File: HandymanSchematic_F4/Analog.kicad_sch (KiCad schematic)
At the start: 38 parts, among them Q1 BC847, U2 TL074, U6 TL072

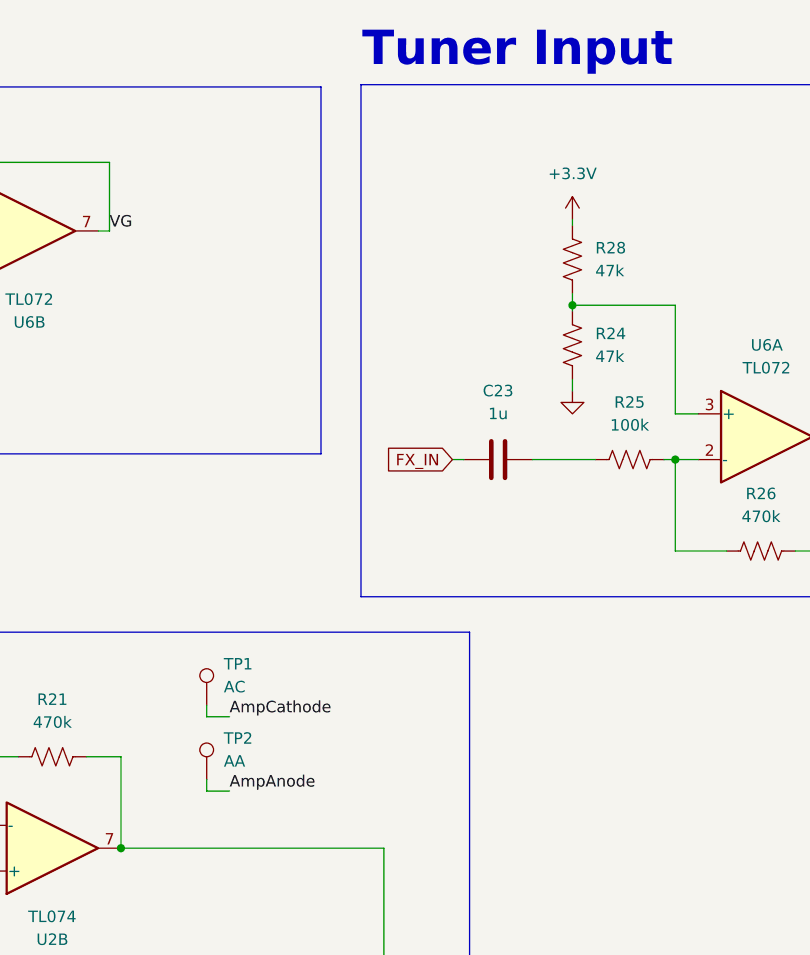
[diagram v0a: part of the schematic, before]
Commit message: schem changes for new display
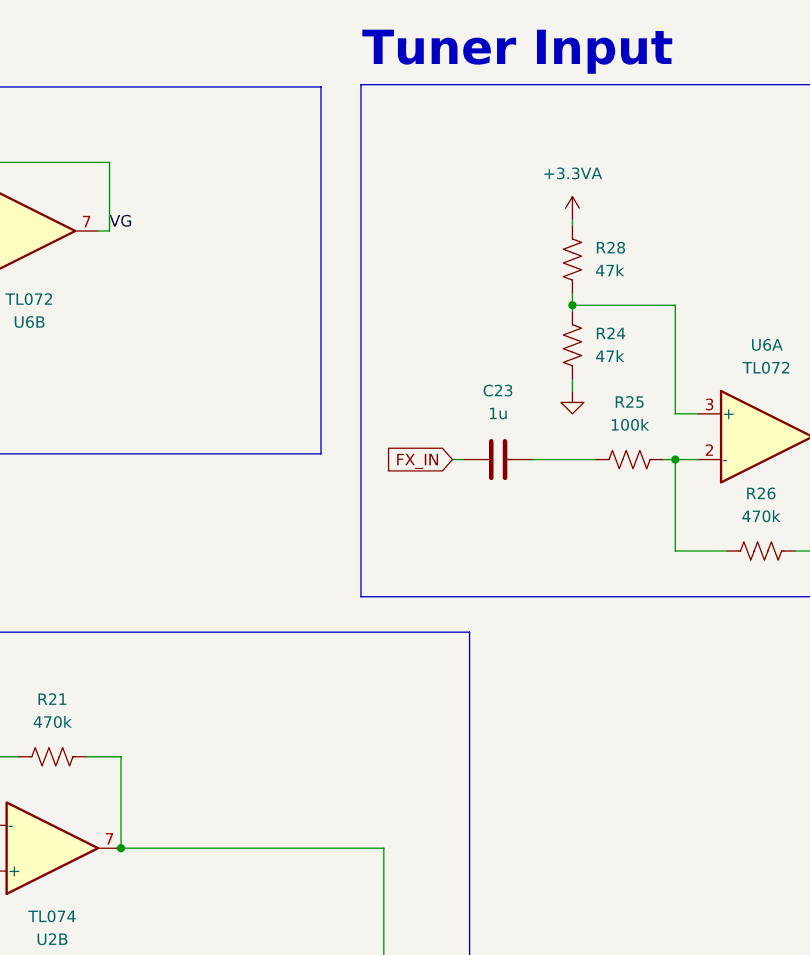
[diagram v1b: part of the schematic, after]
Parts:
- removed TP1: AC, TestPoint:TestPoint_THTPad_D2.0mm_Drill1.0mm_VAL, symbol Connector:TestPoint
- removed TP2: AA, TestPoint:TestPoint_THTPad_D2.0mm_Drill1.0mm_VAL, symbol Connector:TestPoint
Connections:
- net +3.3V: no longer R28.1
- new net +3.3VA: R28.1
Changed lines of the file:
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@@
 	(wire
 		(pts
-			(xy 171.45 90.805) (xy 171.45 89.535)
-		)
-		(stroke
-			(width 0)
-			(type default)
-		)
-	)
-	(wire
-		(pts
-			(xy 173.99 90.805) (xy 171.45 90.805)
-		)
-		(stroke
-			(width 0)
-			(type default)
-		)
-	)
-	(wire
-		(pts
 			(xy 103.505 33.02) (xy 108.585 33.02)
 		)
@@
 	(wire
 		(pts
-			(xy 171.45 99.06) (xy 171.45 97.79)
-		)
-		(stroke
-			(width 0)
-			(type default)
-		)
-	)
-	(wire
-		(pts
 			(xy 89.535 112.395) (xy 89.535 113.665)
 		)
@@
 		)
 	)
-	(wire
-		(pts
-			(xy 173.99 99.06) (xy 171.45 99.06)
-		)
-		(stroke
-			(width 0)
-			(type default)
-		)
-	)
 	(label "VG"
 		(at 103.505 105.41 180)
@@
 	)
 	(label "AmpAnode"
-		(at 173.99 99.06 0)
-		(effects
-			(font
-				(size 1.27 1.27)
-			)
-			(justify left bottom)
-		)
-	)
-	(label "AmpAnode"
 		(at 133.985 153.67 180)
 		(effects
@@
 		)
 	)
-	(label "AmpCathode"
-		(at 173.99 90.805 0)
-		(effects
-			(font
-				(size 1.27 1.27)
-			)
-			(justify left bottom)
-		)
-	)
 	(label "VG"
 		(at 160.655 36.83 0)
@@
 	)
 	(symbol
-		(lib_id "Connector:TestPoint")
-		(at 171.45 89.535 0)
-		(unit 1)
-		(body_style 1)
-		(exclude_from_sim no)
-		(in_bom no)
-		(on_board yes)
-		(in_pos_files yes)
-		(dnp no)
-		(fields_autoplaced yes)
-		(property "Reference" "TP1"
-			(at 173.355 84.9629 0)
-			(show_name no)
-			(do_not_autoplace no)
-			(effects
-				(font
-					(size 1.27 1.27)
-				)
-				(justify left)
-			)
-		)
-		(property "Value" "AC"
-			(at 173.355 87.5029 0)
-			(show_name no)
-			(do_not_autoplace no)
-			(effects
-				(font
-					(size 1.27 1.27)
-				)
-				(justify left)
-			)
-		)
-		(property "Footprint" "TestPoint:TestPoint_THTPad_D2.0mm_Drill1.0mm_VAL"
-			(at 176.53 89.535 0)
-			(hide yes)
-			(show_name no)
-			(do_not_autoplace no)
-			(effects
-				(font
-					(size 1.27 1.27)
-				)
-			)
-		)
-		(property "Datasheet" ""
-			(at 176.53 89.535 0)
-			(hide yes)
-			(show_name no)
-			(do_not_autoplace no)
-			(effects
-				(font
-					(size 1.27 1.27)
-				)
-			)
-		)
-		(property "Description" "test point"
-			(at 171.45 89.535 0)
-			(hide yes)
-			(show_name no)
-			(do_not_autoplace no)
-			(effects
-				(font
-					(size 1.27 1.27)
-				)
-			)
-		)
-		(pin "1"
-		)
-		(instances
-			(project "HandymanSchematic_F4"
-				(path "/bc3da82e-d0a7-49a6-b9ec-ecd2040670ff/3aa5a90d-1712-4ed6-8a31-c8d55dd0f37d"
-					(reference "TP1")
-					(unit 1)
-				)
-			)
-		)
-	)
-	(symbol
 		(lib_id "Device:R_US")
 		(at 131.445 44.45 0)
@@
 	)
 	(symbol
-		(lib_id "Connector:TestPoint")
-		(at 171.45 97.79 0)
-		(unit 1)
-		(body_style 1)
-		(exclude_from_sim no)
-		(in_bom no)
-		(on_board yes)
-		(in_pos_files yes)
-		(dnp no)
-		(fields_autoplaced yes)
-		(property "Reference" "TP2"
-			(at 173.355 93.2179 0)
-			(show_name no)
-			(do_not_autoplace no)
-			(effects
-				(font
-					(size 1.27 1.27)
-				)
-				(justify left)
-			)
-		)
-		(property "Value" "AA"
-			(at 173.355 95.7579 0)
-			(show_name no)
-			(do_not_autoplace no)
-			(effects
-				(font
-					(size 1.27 1.27)
-				)
-				(justify left)
-			)
-		)
-		(property "Footprint" "TestPoint:TestPoint_THTPad_D2.0mm_Drill1.0mm_VAL"
-			(at 176.53 97.79 0)
-			(hide yes)
-			(show_name no)
-			(do_not_autoplace no)
-			(effects
-				(font
-					(size 1.27 1.27)
-				)
-			)
-		)
-		(property "Datasheet" ""
-			(at 176.53 97.79 0)
-			(hide yes)
-			(show_name no)
-			(do_not_autoplace no)
-			(effects
-				(font
-					(size 1.27 1.27)
-				)
-			)
-		)
-		(property "Description" "test point"
-			(at 171.45 97.79 0)
-			(hide yes)
-			(show_name no)
-			(do_not_autoplace no)
-			(effects
-				(font
-					(size 1.27 1.27)
-				)
-			)
-		)
-		(pin "1"
-		)
-		(instances
-			(project "HandymanSchematic_F4"
-				(path "/bc3da82e-d0a7-49a6-b9ec-ecd2040670ff/3aa5a90d-1712-4ed6-8a31-c8d55dd0f37d"
-					(reference "TP2")
-					(unit 1)
-				)
-			)
-		)
-	)
-	(symbol
 		(lib_id "power:GND")
 		(at 71.12 48.895 0)
@@
 	)
 	(symbol
-		(lib_id "power:+3.3V")
-		(at 212.09 35.56 0)
-		(unit 1)
-		(body_style 1)
-		(exclude_from_sim no)
-		(in_bom yes)
-		(on_board yes)
-		(in_pos_files yes)
-		(dnp no)
-		(fields_autoplaced yes)
-		(property "Reference" "#PWR018"
-			(at 212.09 39.37 0)
-			(hide yes)
-			(show_name no)
-			(do_not_autoplace no)
-			(effects
-				(font
-					(size 1.27 1.27)
-				)
-			)
-		)
-		(property "Value" "+3.3V"
-			(at 212.09 30.48 0)
-			(show_name no)
-			(do_not_autoplace no)
-			(effects
-				(font
-					(size 1.27 1.27)
-				)
-			)
-		)
-		(property "Footprint" ""
-			(at 212.09 35.56 0)
-			(hide yes)
-			(show_name no)
-			(do_not_autoplace no)
-			(effects
-				(font
-					(size 1.27 1.27)
-				)
-			)
-		)
-		(property "Datasheet" ""
-			(at 212.09 35.56 0)
-			(hide yes)
-			(show_name no)
-			(do_not_autoplace no)
-			(effects
-				(font
-					(size 1.27 1.27)
-				)
-			)
-		)
-		(property "Description" "Power symbol creates a global label with name \"+3.3V\""
-			(at 212.09 35.56 0)
-			(hide yes)
-			(show_name no)
-			(do_not_autoplace no)
-			(effects
-				(font
-					(size 1.27 1.27)
-				)
-			)
-		)
-		(pin "1"
-		)
-		(instances
-			(project "HandymanSchematic_F4"
-				(path "/bc3da82e-d0a7-49a6-b9ec-ecd2040670ff/3aa5a90d-1712-4ed6-8a31-c8d55dd0f37d"
-					(reference "#PWR018")
-					(unit 1)
-				)
-			)
-		)
-	)
-	(symbol
 		(lib_id "Diode:1N4148W")
 		(at 121.285 127 90)
@@
 					(unit 1)
 				)
+			)
+		)
+	)
+	(symbol
+		(lib_id "power:+3.3VA")
+		(at 212.09 35.56 0)
+		(unit 1)
+		(body_style 1)
+		(exclude_from_sim no)
+		(in_bom yes)
+		(on_board yes)
+		(in_pos_files yes)
+		(dnp no)
+		(fields_autoplaced yes)
+		(property "Reference" "#PWR04"
+			(at 212.09 39.37 0)
+			(hide yes)
+			(show_name no)
+			(do_not_autoplace no)
+			(effects
+				(font
+					(size 1.27 1.27)
+				)
+			)
+		)
+		(property "Value" "+3.3VA"
+			(at 212.09 30.48 0)
+			(show_name no)
+			(do_not_autoplace no)
+			(effects
+				(font
+					(size 1.27 1.27)
+				)
+			)
+		)
+		(property "Footprint" ""
+			(at 212.09 35.56 0)
+			(hide yes)
+			(show_name no)
+			(do_not_autoplace no)
+			(effects
+				(font
+					(size 1.27 1.27)
+				)
+			)
+		)
+		(property "Datasheet" ""
+			(at 212.09 35.56 0)
+			(hide yes)
+			(show_name no)
+			(do_not_autoplace no)
+			(effects
+				(font
+					(size 1.27 1.27)
+				)
+			)
+		)
+		(property "Description" "Power symbol creates a global label with name \"+3.3VA\""
+			(at 212.09 35.56 0)
+			(hide yes)
+			(show_name no)
+			(do_not_autoplace no)
+			(effects
+				(font
+					(size 1.27 1.27)
+				)
+			)
+		)
+		(pin "1"
+		)
+		(instances
+			(project "HandymanSchematic_F4"
+				(path "/bc3da82e-d0a7-49a6-b9ec-ecd2040670ff/3aa5a90d-1712-4ed6-8a31-c8d55dd0f37d"
+					(reference "#PWR04")
+					(unit 1)
+				)

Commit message: beginnings of new layout
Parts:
- RV1, RV2: footprint Potentiometer_THT:Potentiometer_Alpha_RV16AF_42_Single_Long -> Potentiometer_THT:Potentiometer_Alpha_RD901F-40-00D_Single_Vertical_CircularHoles
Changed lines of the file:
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@@
 			)
 		)
-		(property "Footprint" "Potentiometer_THT:Potentiometer_Alpha_RV16AF_42_Single_Long"
+		(property "Footprint" "Potentiometer_THT:Potentiometer_Alpha_RD901F-40-00D_Single_Vertical_CircularHoles"
 			(at 71.12 43.18 0)
 			(hide yes)
@@
 			)
 		)
-		(property "Footprint" "Potentiometer_THT:Potentiometer_Alpha_RV16AF_42_Single_Long"
+		(property "Footprint" "Potentiometer_THT:Potentiometer_Alpha_RD901F-40-00D_Single_Vertical_CircularHoles"
 			(at 31.75 43.815 0)
 			(hide yes)

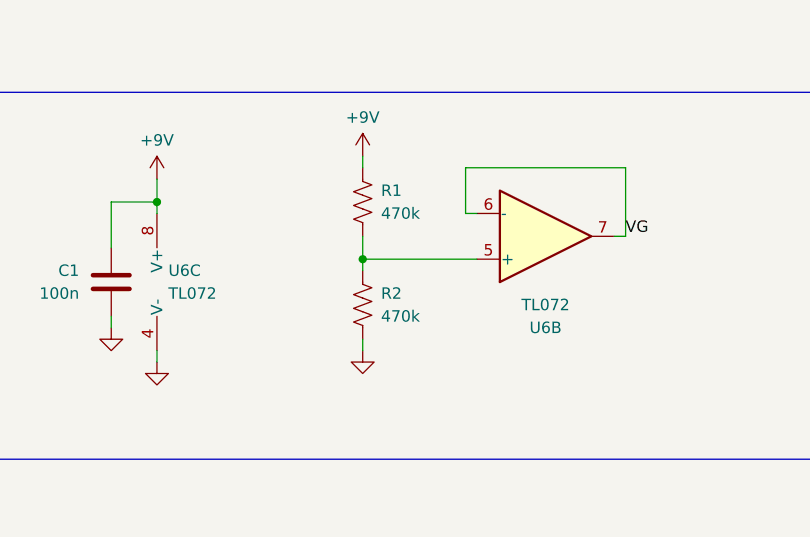
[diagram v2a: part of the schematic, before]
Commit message: corner bevels, silkscreen spacing
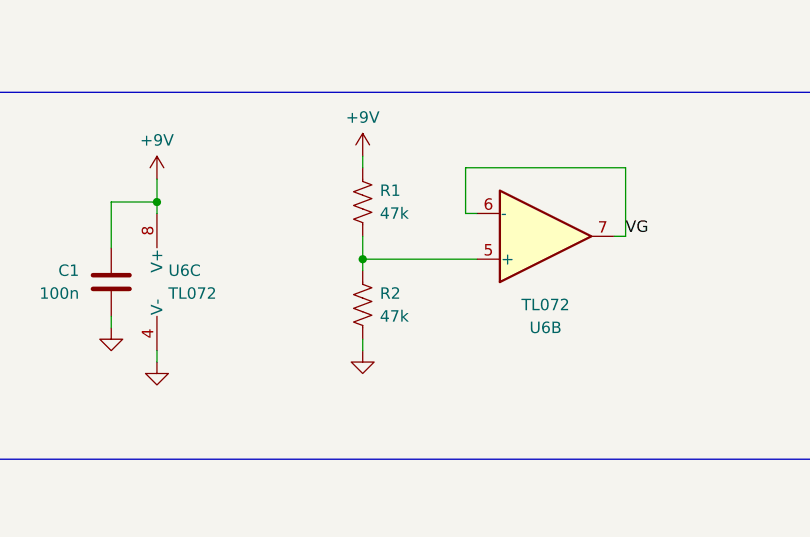
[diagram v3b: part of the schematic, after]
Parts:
- R1, R2: value 470k -> 47k
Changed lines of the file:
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@@
 		(fields_autoplaced yes)
 		(property "Reference" "R1"
-			(at 133.477 31.7499 0)
+			(at 133.35 31.7499 0)
 			(show_name no)
 			(do_not_autoplace no)
@@
 			)
 		)
-		(property "Value" "470k"
-			(at 133.477 34.2899 0)
+		(property "Value" "47k"
+			(at 133.35 34.2899 0)
 			(show_name no)
 			(do_not_autoplace no)
@@
 		(fields_autoplaced yes)
 		(property "Reference" "R2"
-			(at 133.477 43.1799 0)
+			(at 133.35 43.1799 0)
 			(show_name no)
 			(do_not_autoplace no)
@@
 			)
 		)
-		(property "Value" "470k"
-			(at 133.477 45.7199 0)
-			(show_name no)
-			(do_not_autoplace no)
+		(property "Value" "47k"
+			(at 133.35 45.7199 0)
+			(show_name no)
+			(do_not_autoplace no)
